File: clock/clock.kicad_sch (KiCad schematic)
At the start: 6 parts, among them U1 LM555xM

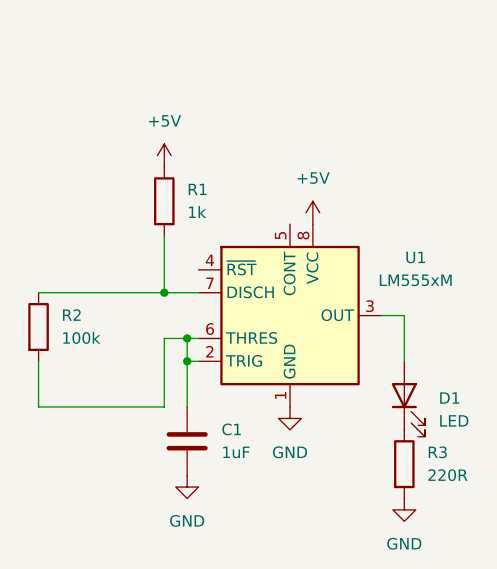
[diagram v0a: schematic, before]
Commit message: fixed wiring, tied pin 4 to high, and pin 5 to capacitor
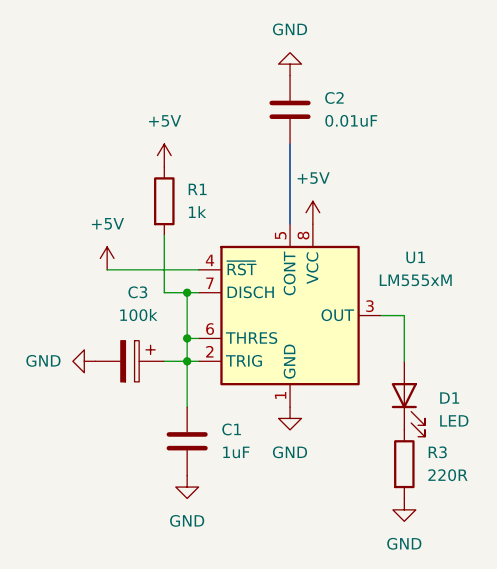
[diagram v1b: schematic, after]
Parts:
- removed R2: 100k, Package_DIP:DIP-8_W7.62mm, symbol Device:R
- added C2: 0.01uF, symbol Device:C
- added C3: 100k, symbol Device:C_Polarized
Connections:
- net +5V: now also U1.4 (~{RST})
- net GND: now also C2.1, C3.2
- net at R1.2, U1.7 (DISCH): now also C1.1, U1.2 (TRIG), U1.6 (THRES), C3.1

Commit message: fixed wiring...
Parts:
- removed C1: 1uF, symbol Device:C
- removed C3: 100k, symbol Device:C_Polarized
- added C1: 1uF, Package_DIP:DIP-24_W7.62mm, symbol Device:C_Polarized
- added R2: 200k, symbol Device:R
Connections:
- net GND: now also C1.2
- net at C2.2: now also U1.5 (CONT)
- net at R1.2, U1.2 (TRIG), U1.6 (THRES)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: now also C1.1, R2.1, R2.2

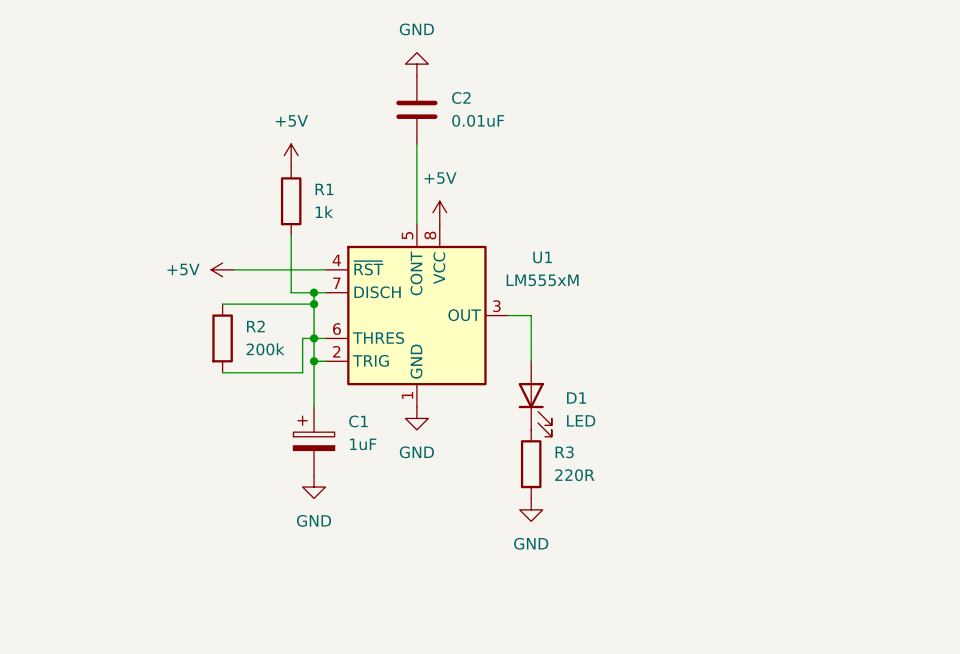
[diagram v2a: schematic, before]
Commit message: second 555 timer to trigger clock included
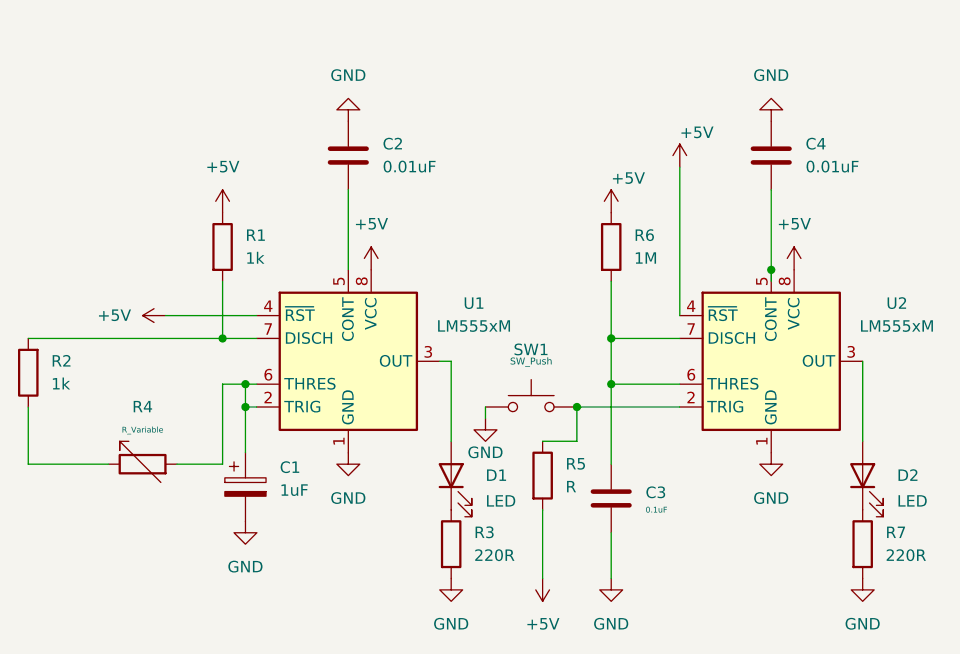
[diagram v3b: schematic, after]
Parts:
- added C3: 0.1uF, Package_SO:SOIC-8_3.9x4.9mm_P1.27mm, symbol Device:C
- added C4: 0.01uF, symbol Device:C
- added D2: LED, symbol Device:LED
- added R4: R_Variable, Package_DFN_QFN:DFN-10-1EP_3x3mm_P0.5mm_EP1.55x2.48mm, symbol Device:R_Variable
- added R5: R, symbol Device:R
- added R6: 1M, symbol Device:R
- added R7: 220R, Package_DIP:DIP-8_W7.62mm, symbol Device:R
- added SW1: SW_Push, Button_Switch_THT:SW_PUSH_6mm_H7.3mm, symbol Switch:SW_Push
- added U2: LM555xM, Package_SO:SOIC-8_3.9x4.9mm_P1.27mm, symbol Timer:LM555xM
- R2: value 200k -> 1k
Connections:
- net +5V: now also R5.2, R6.1, U2.4 (~{RST}), U2.8 (VCC)
- net GND: now also C3.2, C4.1, R7.2, SW1.1, U2.1 (GND)
- new net: C4.2, U2.5 (CONT)
- new net: R5.1, SW1.2, U2.2 (TRIG)
- new net: D2.2 (A), U2.3 (OUT)
- new net: C3.1, R6.2, U2.6 (THRES), U2.7 (DISCH)
- new net: R2.1, R4.1
- new net: R1.2, R2.2, U1.7 (DISCH)
- new net: C1.1, R4.2, U1.2 (TRIG), U1.6 (THRES)
- new net: D2.1 (K), R7.1
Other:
- moved on the sheet: C1, C2, D1, R1, R2, R3, U1

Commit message: Almost done
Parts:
- added C5: 0.01uF, Package_SO:SOIC-8_3.9x4.9mm_P1.27mm, symbol Device:C
- added D3, D4: LED, symbol Device:LED
- added R10: 220R, Package_DIP:DIP-8_W7.62mm, symbol Device:R
- added R8, R9: 1k, Package_DIP:DIP-8_W7.62mm, symbol Device:R
- added SW2: SW_SPDT, Button_Switch_THT:SW_NKK_NR01, symbol Switch:SW_SPDT
- added U3: LM555xM, Package_SO:SOIC-8_3.9x4.9mm_P1.27mm, symbol Timer:LM555xM
- added U4: 74LS04, Package_CSP:Xilinx_CSG48_7.0x7.0mm_Layout7x7_P0.8mm, symbol 74xx:74LS04
- added U5: 74LS08, Package_DIP:DIP-14_W7.62mm, symbol 74xx:74LS08
- added U6: 74LS32, Package_CSP:Xilinx_CSG48_7.0x7.0mm_Layout7x7_P0.8mm, symbol 74xx:74LS32
- R5: value R -> 1K
- renumbered R2 to R1, R4 to R2, R1 to R3, R3 to R4
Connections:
- net +5V: now also U3.8 (VCC), U4.14 (VCC), U5.14 (VCC), U6.14 (VCC)
- net GND: now also C5.1, R10.2, R8.1, R9.2, SW2.2 (B), U3.1 (GND), U3.6 (THRES), U4.7 (GND), U4.9, U5.7 (GND), U6.7 (GND)
- net at D2.2 (A), U2.3 (OUT): now also U5.5
- net at D1.2 (A), U1.3 (OUT): now also U5.2
- new net: R9.1, SW2.1 (A), U3.2 (TRIG)
- new net: D3.2 (A), U3.3 (OUT), U4.1, U5.1
- new net: R8.2, SW2.3 (C), U3.4 (~{RST})
- new net: C5.2, U3.5 (CONT)
- new net: U4.2, U5.4
- new net: U5.6, U6.2
- new net: U4.8, U5.10
- new net: D3.1 (K), R10.1
- new net: U5.3, U6.1
- new net: U5.9, U6.3
- new net: D4.2 (A), U5.8
